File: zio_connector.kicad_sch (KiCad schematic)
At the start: 4 parts, among them CN10 Conn_02x17_Odd_Even, CN7 Conn_02x10_Odd_Even, CN8 Conn_02x08_Odd_Even, CN9 Conn_02x15_Odd_Even

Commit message: CAN1 finished
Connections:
- net PB12 is gone; now on net CAN1_STB: CN7.7 (Pin_7)
- net CAN1_STB: no longer CN7.3 (Pin_3)
- net CAN2_RX: no longer CN7.14 (Pin_14)
- new net PB15: CN7.3 (Pin_3)
- no-connect marks 8 -> 10
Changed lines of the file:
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@@
 	(paper "A4")
 	(no_connect
+		(at 144.78 40.64)
+	)
+	(no_connect
 		(at 133.35 95.25)
 	)
@@
 	)
 	(no_connect
+		(at 157.48 40.64)
+	)
+	(no_connect
 		(at 146.05 97.79)
 	)
@@
 	(wire
 		(pts
+			(xy 116.84 33.02) (xy 132.08 33.02)
+		)
+		(stroke
+			(width 0)
+			(type default)
+		)
+	)
+	(wire
+		(pts
 			(xy 146.05 69.85) (xy 158.75 69.85)
 		)
@@
 	(wire
 		(pts
+			(xy 119.38 27.94) (xy 132.08 27.94)
+		)
+		(stroke
+			(width 0)
+			(type default)
+		)
+	)
+	(wire
+		(pts
 			(xy 74.93 36.83) (xy 82.55 36.83)
 		)
@@
 	(wire
 		(pts
-			(xy 119.38 33.02) (xy 132.08 33.02)
-		)
-		(stroke
-			(width 0)
-			(type default)
-		)
-	)
-	(wire
-		(pts
 			(xy 132.08 69.85) (xy 133.35 69.85)
 		)
@@
 	(wire
 		(pts
-			(xy 116.84 27.94) (xy 132.08 27.94)
-		)
-		(stroke
-			(width 0)
-			(type default)
-		)
-	)
-	(wire
-		(pts
 			(xy 73.66 78.74) (xy 74.93 78.74)
 		)
@@
 		(pts
 			(xy 73.66 101.6) (xy 90.17 101.6)
-		)
-		(stroke
-			(width 0)
-			(type default)
-		)
-	)
-	(wire
-		(pts
-			(xy 144.78 40.64) (xy 157.48 40.64)
 		)
 		(stroke
@@
 	(global_label "CAN1_STB"
 		(shape input)
-		(at 116.84 27.94 180)
+		(at 116.84 33.02 180)
 		(fields_autoplaced yes)
 		(effects
@@
 		)
 		(property "Intersheetrefs" "${INTERSHEET_REFS}"
-			(at 104.5415 27.94 0)
+			(at 104.5415 33.02 0)
 			(effects
 				(font

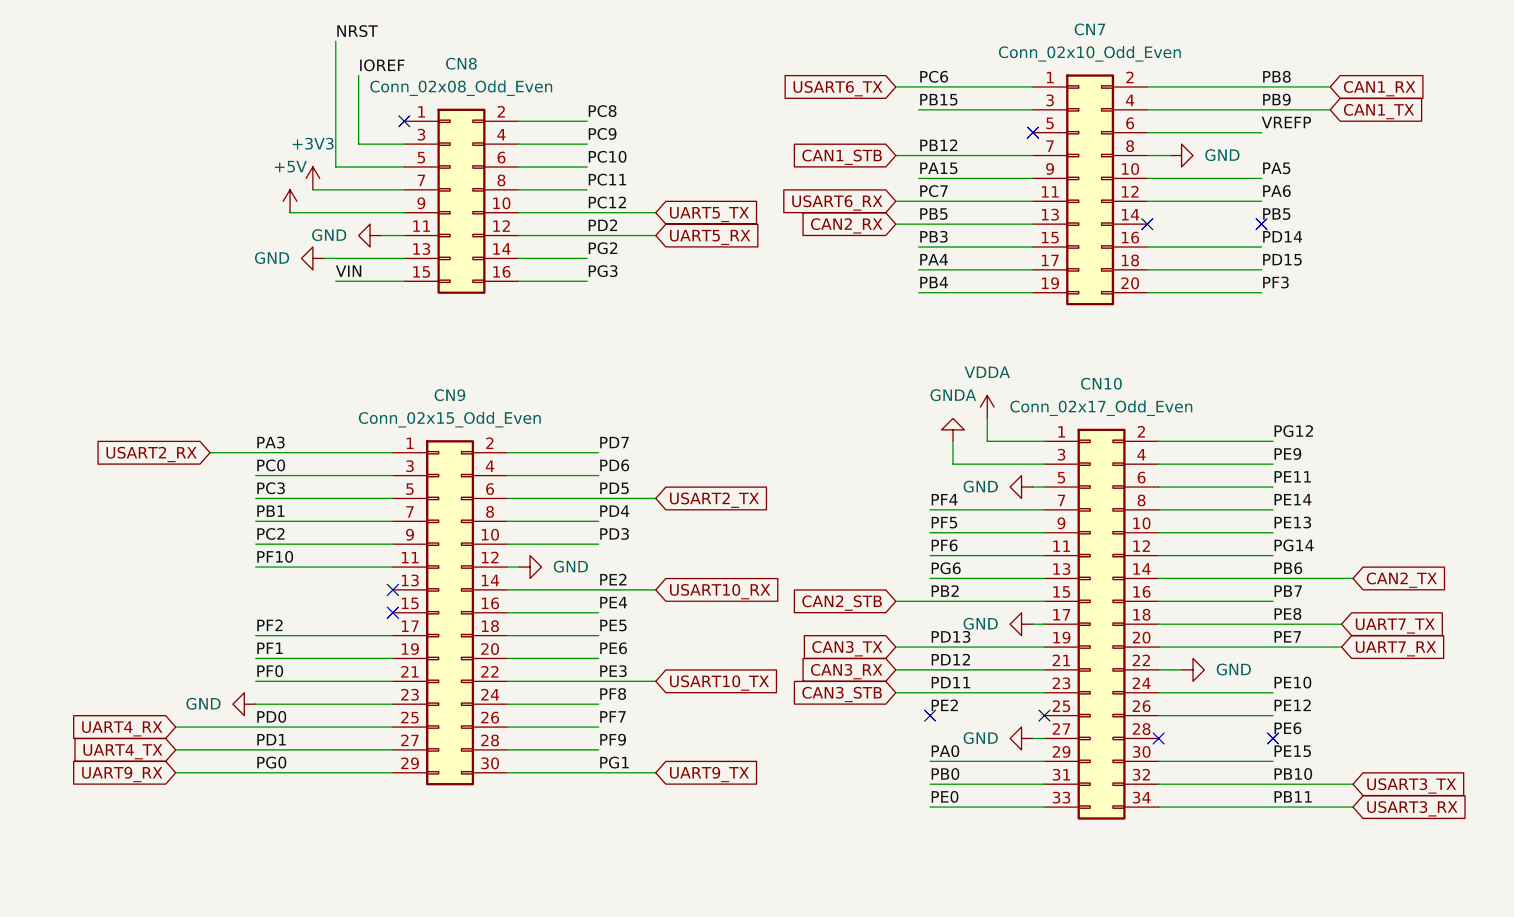
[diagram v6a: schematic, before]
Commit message: All nets conected except GND, +3V3, +5V
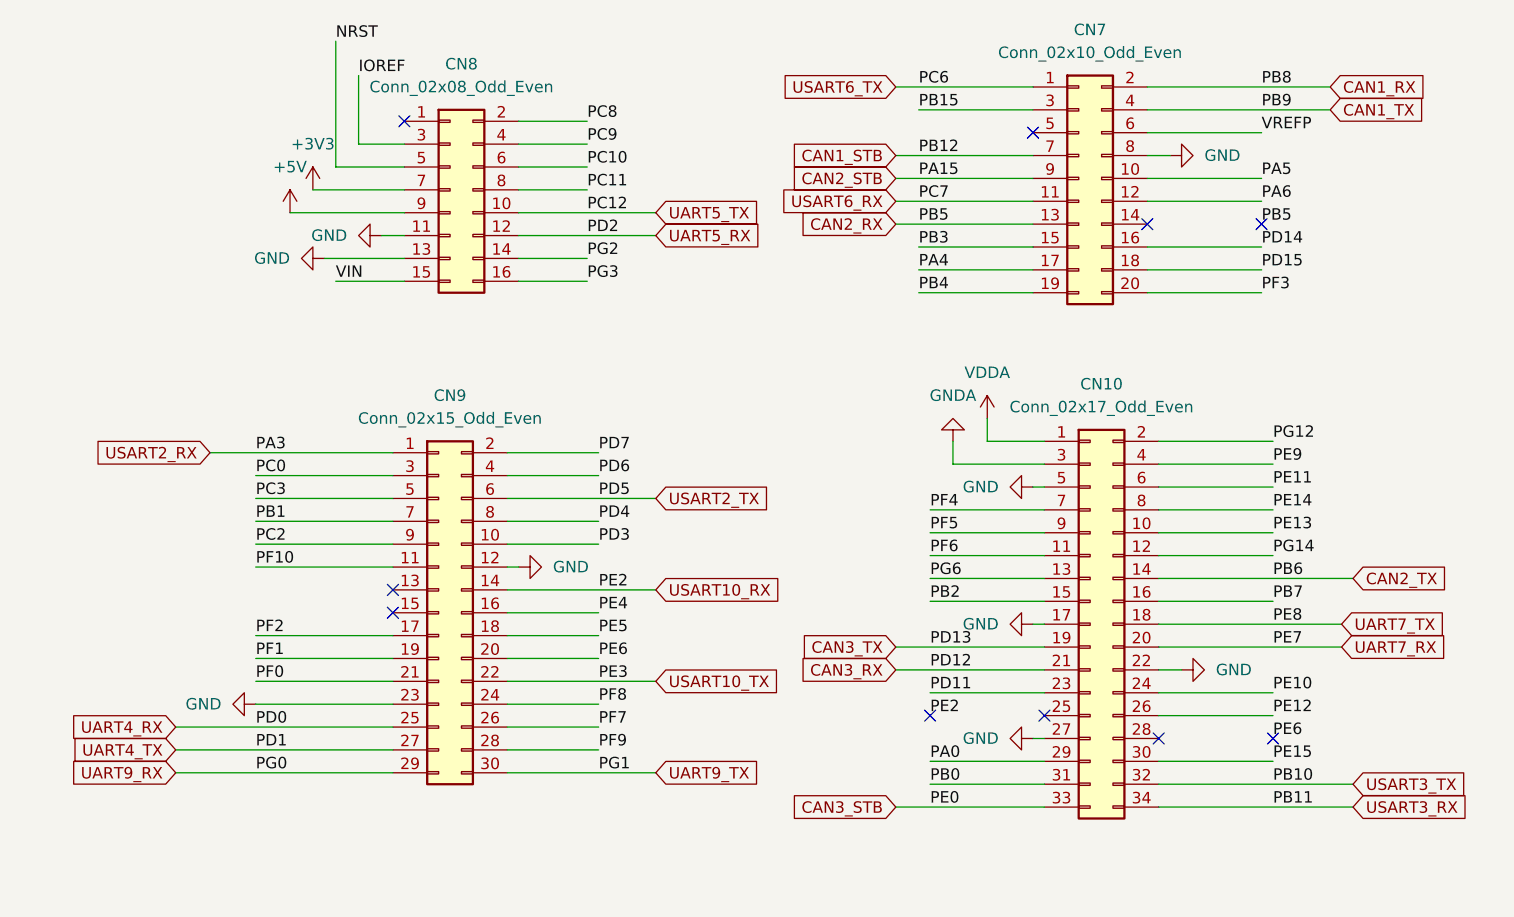
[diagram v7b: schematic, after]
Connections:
- net PA15 is gone; now on net CAN2_STB: CN7.9 (Pin_9)
- net PE0 is gone; now on net CAN3_STB: CN10.33 (Pin_33)
- net CAN2_STB: no longer CN10.15 (Pin_15)
- net CAN3_STB: no longer CN10.23 (Pin_23)
- new net PB2: CN10.15 (Pin_15)
- new net PD11: CN10.23 (Pin_23)
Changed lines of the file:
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@@
 	(wire
 		(pts
-			(xy 119.38 35.56) (xy 132.08 35.56)
+			(xy 116.84 105.41) (xy 133.35 105.41)
 		)
 		(stroke
@@
 	(wire
 		(pts
-			(xy 116.84 92.71) (xy 133.35 92.71)
-		)
-		(stroke
-			(width 0)
-			(type default)
-		)
-	)
-	(wire
-		(pts
 			(xy 116.84 38.1) (xy 132.08 38.1)
 		)
@@
 	(wire
 		(pts
+			(xy 120.65 82.55) (xy 133.35 82.55)
+		)
+		(stroke
+			(width 0)
+			(type default)
+		)
+	)
+	(wire
+		(pts
 			(xy 146.05 69.85) (xy 158.75 69.85)
 		)
@@
 	(wire
 		(pts
+			(xy 120.65 92.71) (xy 133.35 92.71)
+		)
+		(stroke
+			(width 0)
+			(type default)
+		)
+	)
+	(wire
+		(pts
 			(xy 74.93 36.83) (xy 82.55 36.83)
 		)
@@
 	(wire
 		(pts
+			(xy 116.84 35.56) (xy 132.08 35.56)
+		)
+		(stroke
+			(width 0)
+			(type default)
+		)
+	)
+	(wire
+		(pts
 			(xy 45.72 76.2) (xy 60.96 76.2)
 		)
@@
 	(wire
 		(pts
-			(xy 116.84 82.55) (xy 133.35 82.55)
-		)
-		(stroke
-			(width 0)
-			(type default)
-		)
-	)
-	(wire
-		(pts
 			(xy 146.05 102.87) (xy 167.64 102.87)
 		)
@@
 		(pts
 			(xy 45.72 71.12) (xy 60.96 71.12)
-		)
-		(stroke
-			(width 0)
-			(type default)
-		)
-	)
-	(wire
-		(pts
-			(xy 120.65 105.41) (xy 133.35 105.41)
 		)
 		(stroke
@@
 	(global_label "CAN3_STB"
 		(shape input)
-		(at 116.84 92.71 180)
+		(at 116.84 105.41 180)
 		(fields_autoplaced yes)
 		(effects
@@
 		)
 		(property "Intersheetrefs" "${INTERSHEET_REFS}"
-			(at 104.5415 92.71 0)
+			(at 104.5415 105.41 0)
 			(effects
 				(font
@@
 	(global_label "CAN2_STB"
 		(shape input)
-		(at 116.84 82.55 180)
+		(at 116.84 35.56 180)
 		(fields_autoplaced yes)
 		(effects
@@
 		)
 		(property "Intersheetrefs" "${INTERSHEET_REFS}"
-			(at 104.5415 82.55 0)
-			(effects
-				(font
+			(at 104.5415 35.56 0)
+			(effects
+				(font
